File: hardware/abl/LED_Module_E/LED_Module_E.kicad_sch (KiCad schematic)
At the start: 97 parts, among them J1 SFW20S-2STE1LF, J3 009159008603906, K1 Conn_01x01, K10 Conn_01x01, K11 Conn_01x01, K12 Conn_01x01, K13 Conn_01x01, K14 Conn_01x01, K15 Conn_01x01, K16 Conn_01x01, K17 Conn_01x01, K18 Conn_01x01, K2 Conn_01x01, K3 Conn_01x01, K4 Conn_01x01, K5 Conn_01x01, K6 Conn_01x01, K7 Conn_01x01, K8 Conn_01x01, K9 Conn_01x01, Q1 Si3456DDV, Q11 Si3456DDV, Q12 Si3456DDV, Q2 Si3456DDV, Q3 Si3456DDV, Q4 Si3456DDV, Q5 Si3456DDV, Q6 Si3456DDV, Q7 Si3456DDV, Q8 Si3456DDV, U2 74HC245, U3 24AA025UIDT-I/OT, U4 74LVC1G32

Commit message: Several small fixes
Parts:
- U3: value 24AA025UIDT-I/OT -> 24AA025E48T-I/OT; LCSC Part # C2061498 -> C129895; Manufacturer_Part_Number 24AA025UIDT-I/OT -> 24AA025E48T-I/OT
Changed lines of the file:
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@@
 			)
 		)
-		(property "Value" "24AA025UIDT-I/OT"
+		(property "Value" "24AA025E48T-I/OT"
 			(at 190.1541 38.735 0)
 			(effects
@@
 			)
 		)
-		(property "Datasheet" "http://ww1.microchip.com/downloads/en/DeviceDoc/21709J.pdf"
+		(property "Datasheet" "https://www.lcsc.com/datasheet/lcsc_datasheet_1810121540_Microchip-Tech-24AA025E48T-I-OT_C129895.pdf"
 			(at 187.96 33.02 0)
 			(effects
@@
 			)
 		)
-		(property "Manufacturer_Part_Number" "24AA025UIDT-I/OT"
+		(property "Manufacturer_Part_Number" "24AA025E48T-I/OT"
 			(at 187.96 45.72 0)
 			(effects
@@
 			)
 		)
-		(property "LCSC Part #" "C2061498"
+		(property "LCSC Part #" "C129895"
 			(at 187.96 45.72 0)
 			(effects

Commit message: Many, many minor updates to the big PCBs, and a few simple helper PCBs.
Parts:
- C4: value 680uF -> 1000uF; LCSC Part # C2760485 -> C487313; Manufacturer_Part_Number RVT1A681M0810 680UF 10V -> VKME1301C102MV
- C5: value 680uF -> 1000uF
- H1, H2, H3, H4, H5, H6, K1, K10, K11, K12, K13, K14, K15, K16, K17, K18, K2, K3, K4, K5, K6, K7, K8, K9, LOGO1, TP1, TP10, TP11, TP12, TP13, TP14, TP2, TP3, TP4, TP5, TP6, TP7, TP8, TP9: now not fitted
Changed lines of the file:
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@@
 		(in_bom no)
 		(on_board yes)
-		(dnp no)
+		(dnp yes)
 		(fields_autoplaced yes)
 		(property "Reference" "H5"
@@
 		(in_bom yes)
 		(on_board yes)
-		(dnp no)
+		(dnp yes)
 		(property "Reference" "TP8"
 			(at 100.33 40.005 0)
@@
 		(in_bom no)
 		(on_board yes)
-		(dnp no)
+		(dnp yes)
 		(fields_autoplaced yes)
 		(property "Reference" "H4"
@@
 		(in_bom yes)
 		(on_board yes)
-		(dnp no)
+		(dnp yes)
 		(fields_autoplaced yes)
 		(property "Reference" "K12"
@@
 		(in_bom yes)
 		(on_board yes)
-		(dnp no)
+		(dnp yes)
 		(fields_autoplaced yes)
 		(property "Reference" "K6"
@@
 		(in_bom yes)
 		(on_board yes)
-		(dnp no)
+		(dnp yes)
 		(fields_autoplaced yes)
 		(property "Reference" "K18"
@@
 		(in_bom yes)
 		(on_board yes)
-		(dnp no)
+		(dnp yes)
 		(property "Reference" "TP7"
 			(at 100.33 27.305 0)
@@
 		(in_bom yes)
 		(on_board yes)
-		(dnp no)
+		(dnp yes)
 		(property "Reference" "TP10"
 			(at 100.33 65.405 0)
@@
 		(in_bom yes)
 		(on_board yes)
-		(dnp no)
+		(dnp yes)
 		(fields_autoplaced yes)
 		(property "Reference" "K3"
@@
 		(in_bom yes)
 		(on_board yes)
-		(dnp no)
+		(dnp yes)
 		(fields_autoplaced yes)
 		(property "Reference" "K11"
@@
 		(in_bom yes)
 		(on_board yes)
-		(dnp no)
+		(dnp yes)
 		(fields_autoplaced yes)
 		(property "Reference" "K7"
@@
 		(in_bom yes)
 		(on_board yes)
-		(dnp no)
+		(dnp yes)
 		(fields_autoplaced yes)
 		(property "Reference" "K13"
@@
 		(in_bom yes)
 		(on_board yes)
-		(dnp no)
+		(dnp yes)
 		(property "Reference" "TP14"
 			(at 100.33 116.205 0)
@@
 		(in_bom yes)
 		(on_board yes)
-		(dnp no)
+		(dnp yes)
 		(fields_autoplaced yes)
 		(property "Reference" "K8"
@@
 		(in_bom no)
 		(on_board yes)
-		(dnp no)
+		(dnp yes)
 		(fields_autoplaced yes)
 		(property "Reference" "H2"
@@
 		(in_bom yes)
 		(on_board yes)
-		(dnp no)
+		(dnp yes)
 		(fields_autoplaced yes)
 		(property "Reference" "K15"
@@
 		(in_bom yes)
 		(on_board yes)
-		(dnp no)
+		(dnp yes)
 		(fields_autoplaced yes)
 		(property "Reference" "K17"
@@
 			)
 		)
-		(property "Value" "680uF"
+		(property "Value" "1000uF"
 			(at 151.765 37.8459 0)
 			(effects
@@
 			)
 		)
-		(property "Manufacturer_Part_Number" "RVT1A681M0810 680UF 10V"
+		(property "Manufacturer_Part_Number" "VKME1301C102MV"
 			(at 148.59 37.465 0)
 			(effects
@@
 			)
 		)
-		(property "LCSC Part #" "C2760485"
+		(property "LCSC Part #" "C487313"
 			(at 148.59 37.465 0)
 			(effects
@@
 		(in_bom yes)
 		(on_board yes)
-		(dnp no)
+		(dnp yes)
 		(fields_autoplaced yes)
 		(property "Reference" "K4"
@@
 		(in_bom yes)
 		(on_board yes)
-		(dnp no)
+		(dnp yes)
 		(property "Reference" "TP13"
 			(at 100.33 102.235 0)
@@
 		(in_bom yes)
 		(on_board yes)
-		(dnp no)
+		(dnp yes)
 		(property "Reference" "TP11"
 			(at 100.33 76.835 0)
@@
 		(in_bom no)
 		(on_board yes)
-		(dnp no)
+		(dnp yes)
 		(fields_autoplaced yes)
 		(property "Reference" "H3"
@@
 		(in_bom yes)
 		(on_board yes)
-		(dnp no)
+		(dnp yes)
 		(fields_autoplaced yes)
 		(property "Reference" "K9"
@@
 		(in_bom no)
 		(on_board yes)
-		(dnp no)
+		(dnp yes)
 		(fields_autoplaced yes)
 		(property "Reference" "H1"
@@
 			)
 		)
-		(property "Value" "680uF"
+		(property "Value" "1000uF"
 			(at 132.715 38.1 0)
 			(effects
@@
 		(in_bom no)
 		(on_board yes)
-		(dnp no)
+		(dnp yes)
 		(fields_autoplaced yes)
 		(property "Reference" "H6"
@@
 		(in_bom yes)
 		(on_board yes)
-		(dnp no)
+		(dnp yes)
 		(fields_autoplaced yes)
 		(property "Reference" "K2"
@@
 		(in_bom yes)
 		(on_board yes)
-		(dnp no)
+		(dnp yes)
 		(fields_autoplaced yes)
 		(property "Reference" "K14"
@@
 		(in_bom yes)
 		(on_board yes)
-		(dnp no)
+		(dnp yes)
 		(fields_autoplaced yes)
 		(property "Reference" "K10"
@@
 		(in_bom yes)
 		(on_board yes)
-		(dnp no)
+		(dnp yes)
 		(property "Reference" "TP12"
 			(at 100.33 90.805 0)
@@
 		(in_bom yes)
 		(on_board yes)
-		(dnp no)
+		(dnp yes)
 		(property "Reference" "TP3"
 			(at 109.855 164.465 0)
@@
 		(in_bom yes)
 		(on_board yes)
-		(dnp no)
+		(dnp yes)
 		(property "Reference" "TP5"
 			(at 121.285 164.465 0)
@@
 		(in_bom yes)
 		(on_board yes)
-		(dnp no)
+		(dnp yes)
 		(fields_autoplaced yes)
 		(property "Reference" "K1"
@@
 		(in_bom yes)
 		(on_board yes)
-		(dnp no)
+		(dnp yes)
 		(property "Reference" "TP9"
 			(at 100.33 52.705 0)
@@
 		(in_bom yes)
 		(on_board yes)
-		(dnp no)
+		(dnp yes)
 		(property "Reference" "TP2"
 			(at 104.14 164.465 0)
@@
 		(in_bom yes)
 		(on_board yes)
-		(dnp no)
+		(dnp yes)
 		(property "Reference" "TP4"
 			(at 115.57 164.465 0)
@@
 		(in_bom yes)
 		(on_board yes)
-		(dnp no)
+		(dnp yes)
 		(property "Reference" "TP6"
 			(at 127 164.465 0)
@@
 		(in_bom yes)
 		(on_board yes)
-		(dnp no)
+		(dnp yes)
 		(fields_autoplaced yes)
 		(property "Reference" "K5"
@@
 		(in_bom yes)
 		(on_board yes)
-		(dnp no)
+		(dnp yes)
 		(property "Reference" "TP1"
 			(at 99.06 164.465 0)
@@
 		(in_bom yes)
 		(on_board yes)
-		(dnp no)
+		(dnp yes)
 		(fields_autoplaced yes)
 		(property "Reference" "K16"
@@
 		(in_bom no)
 		(on_board yes)
-		(dnp no)
+		(dnp yes)
 		(fields_autoplaced yes)
 		(property "Reference" "LOGO1"

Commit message: Many small adjustments for the next production run.
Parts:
- removed TP1, TP2, TP3, TP4: TestPoint, TestPoint:TestPoint_Pad_D1.0mm, symbol Connector:TestPoint
- added H7, H8: MountingHole_Pad, MountingHole:MountingHole_2.5mm_Pad_TopOnly, symbol Mechanical:MountingHole_Pad
- C5: LCSC Part # C2760485 -> C487313; Manufacturer_Part_Number RVT1A681M0810 680UF 10V -> VKME1301C102MV
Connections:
- net +5V is gone; now on net +4V: C2.1, J1.13, J3.4, U2.20 (VCC)
- net GND: now also H7.1, H8.1

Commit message: Add missing LCSC part numbers and bump version / date.
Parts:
- J1: LCSC Part # C5407823 -> C3168412
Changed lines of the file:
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@@
 			)
 		)
-		(property "LCSC Part #" "C5407823"
+		(property "LCSC Part #" "C3168412"
 			(at 246.38 52.07 0)
 			(effects

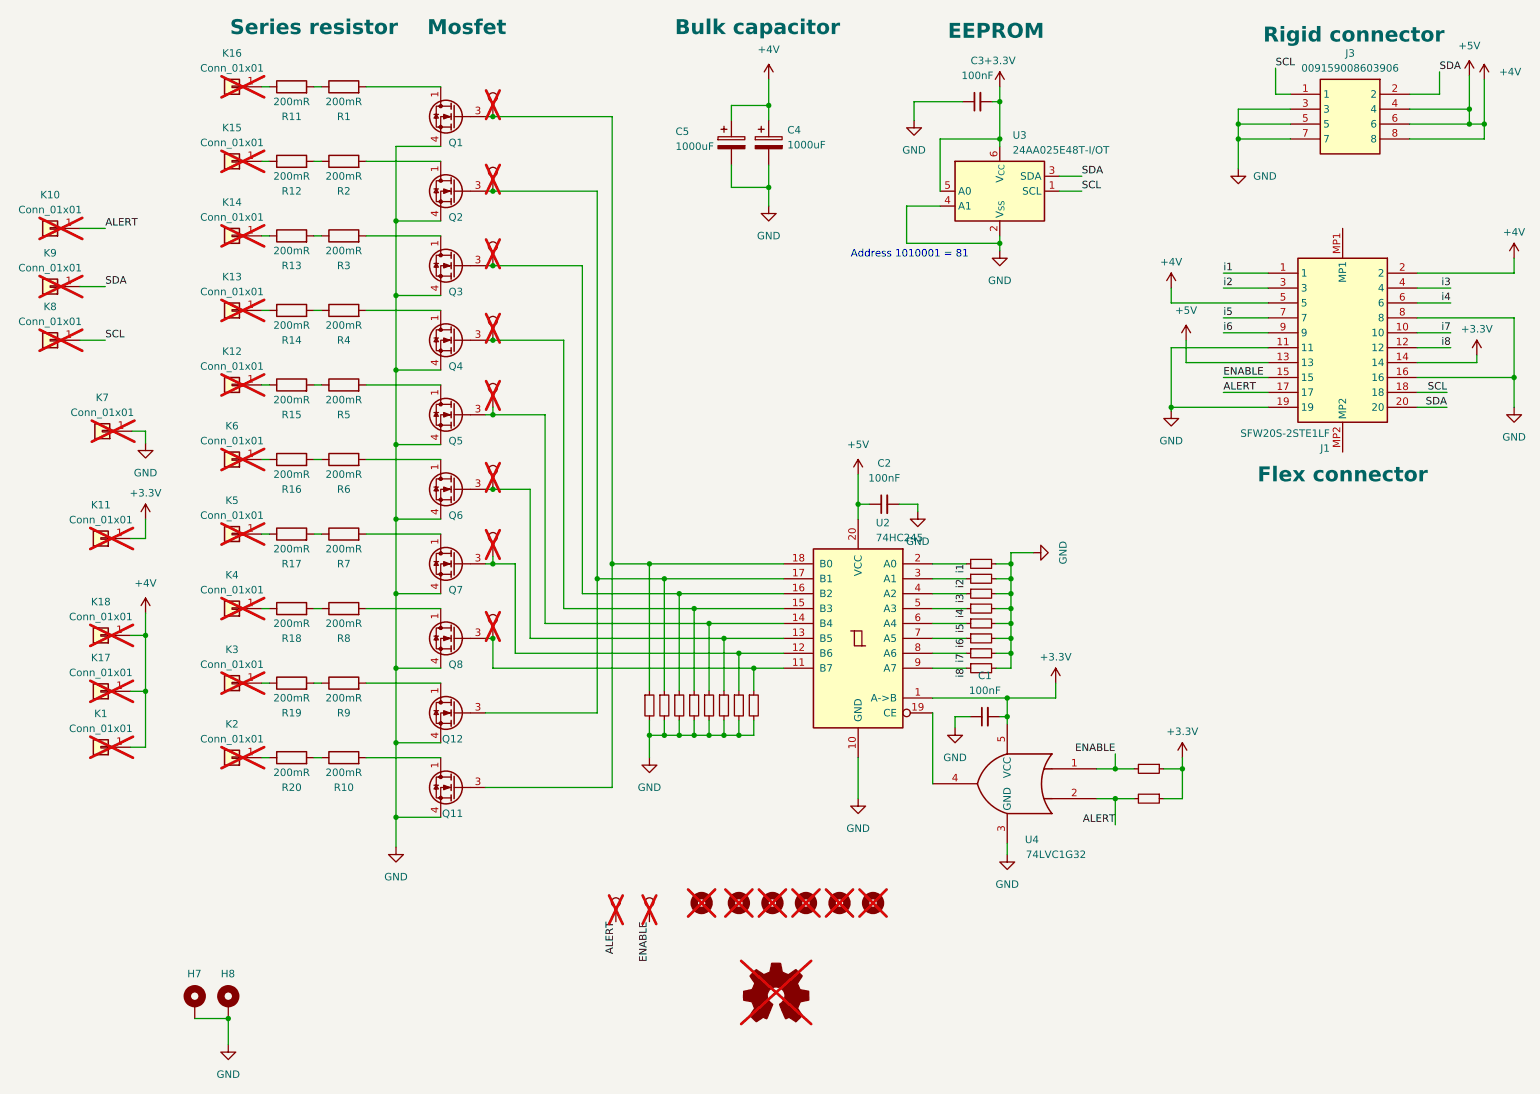
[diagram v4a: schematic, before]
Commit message: Update files and documentation for LED modules E and G.
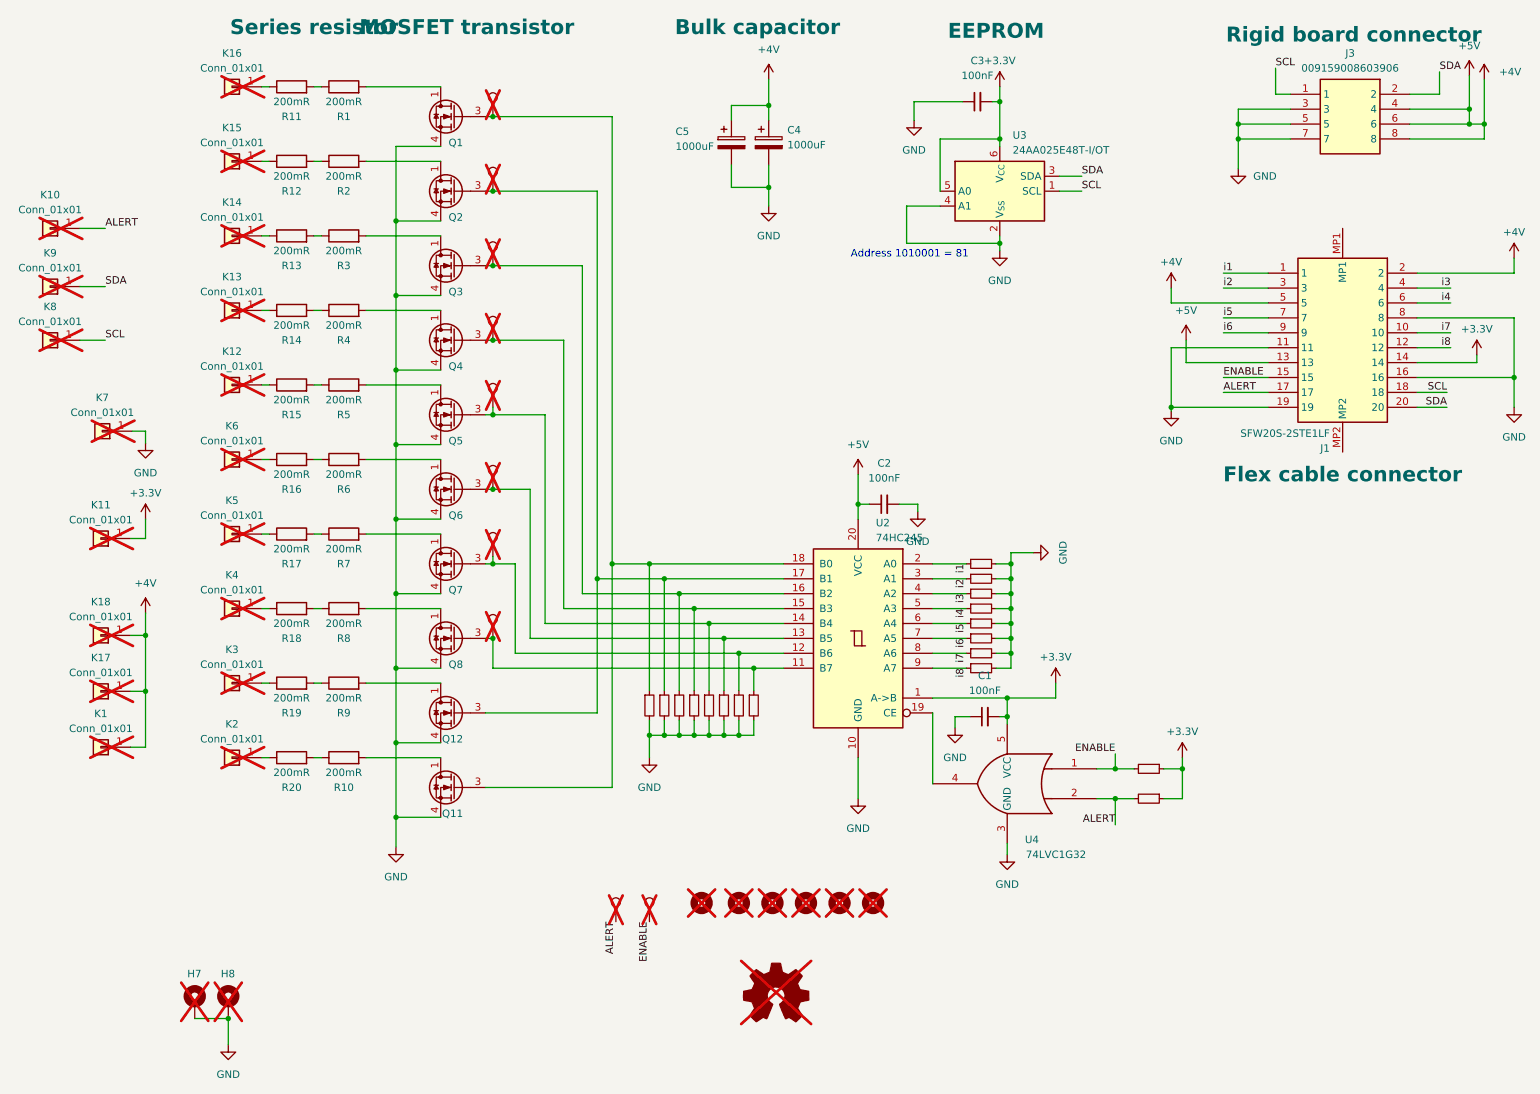
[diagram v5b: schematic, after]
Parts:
- C1, C2, C3: Manufacturer_Part_Number (none) -> CL05B104KO5NNNC
- H7, H8: now not fitted
- J1: Purpose Flex connector -> Flex cable connector
- J3: LCSC Part # (none) -> C22394454; Purpose Rigid connector -> Rigid board connector
- Q1, Q11, Q12, Q2, Q3, Q4, Q5, Q6, Q7, Q8: LCSC Part # C145273 -> C6295864; Manufacturer_Part_Number SI3456DDV-T1-GE3 -> SI3456DDV-T1-BE3; Purpose Mosfet -> MOSFET transistor
- R21, R22, R23, R24, R25, R26, R27, R28, R31, R32, R33, R34, R35, R36, R37, R38: LCSC Part # (none) -> C25900; Manufacturer_Part_Number (none) -> 0402WGF4701TCE; Purpose Pullup -> Pullup resistor
- R40, R41: Purpose Pullup -> Pullup resistor
- U2: Purpose (none) -> Bus transceivers / line driver
- U4: Purpose (none) -> Logic OR gate

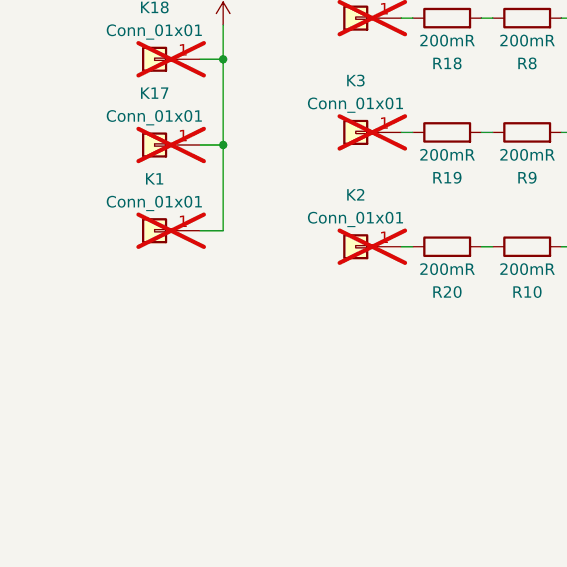
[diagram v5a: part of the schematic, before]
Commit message: LED Module E version 4.0: two rows of castellated holes instead of one, for larger pitch and easier soldering. Also optimized routing.
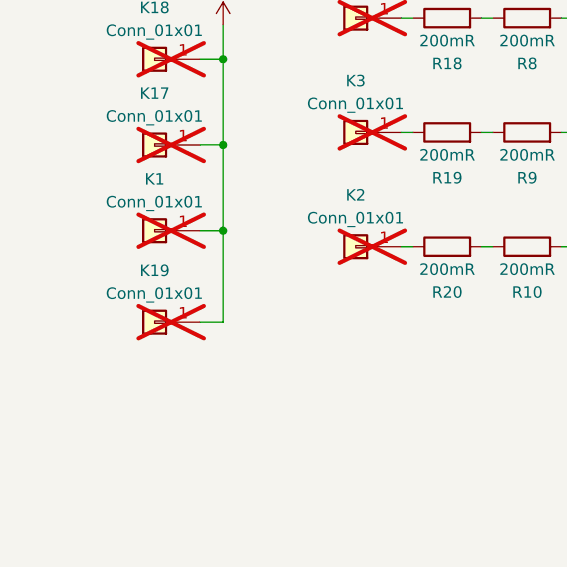
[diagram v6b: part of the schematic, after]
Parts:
- added K19: Conn_01x01, TestPoint:TestPoint_THTPad_1.0x1.0mm_Drill0.5mm, symbol Connector_Generic:Conn_01x01
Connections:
- net +4V: now also K19.1 (Pin_1)
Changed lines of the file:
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@@
 	(title_block
 		(title "besteLampe! LED Module E")
-		(date "2024-12-01")
-		(rev "3.0")
+		(date "2025-09-13")
+		(rev "4.0")
 		(comment 1 "See  https://lenaschimmel.de/besteLampe! for the source and more information")
 		(comment 2 "This source describes Open Hardware and is licensed under the CERN-OHL-S v2.")
@@
 	)
 	(junction
+		(at 42.418 140.462)
+		(diameter 0)
+		(color 0 0 0 0)
+	)
+	(junction
 		(at 101.6 33.02)
 		(diameter 0)
@@
 	(wire
 		(pts
+			(xy 42.418 150.622) (xy 42.418 140.462)
+		)
+		(stroke
+			(width 0)
+			(type default)
+		)
+	)
+	(wire
+		(pts
 			(xy 80.01 91.44) (xy 92.71 91.44)
 		)
@@
 	(wire
 		(pts
+			(xy 39.878 150.622) (xy 42.418 150.622)
+		)
+		(stroke
+			(width 0)
+			(type default)
+		)
+	)
+	(wire
+		(pts
 			(xy 219.075 149.225) (xy 215.9 149.225)
 		)
@@
 					(unit 1)
 				)
+			)
+		)
+	)
+	(symbol
+		(lib_id "Connector_Generic:Conn_01x01")
+		(at 34.798 150.622 180)
+		(unit 1)
+		(exclude_from_sim no)
+		(in_bom yes)
+		(on_board yes)
+		(dnp yes)
+		(fields_autoplaced yes)
+		(property "Reference" "K19"
+			(at 34.798 144.907 0)
+			(effects
+				(font
+					(size 1.27 1.27)
+				)
+			)
+		)
+		(property "Value" "Conn_01x01"
+			(at 34.798 147.447 0)
+			(effects
+				(font
+					(size 1.27 1.27)
+				)
+			)
+		)
+		(property "Footprint" "TestPoint:TestPoint_THTPad_1.0x1.0mm_Drill0.5mm"
+			(at 34.798 150.622 0)
+			(effects
+				(font
+					(size 1.27 1.27)
+				)
+				(hide yes)
+			)
+		)
+		(property "Datasheet" "~"
+			(at 34.798 150.622 0)
+			(effects
+				(font
+					(size 1.27 1.27)
+				)
+				(hide yes)
+			)
+		)
+		(property "Description" "Generic connector, single row, 01x01, script generated (kicad-library-utils/schlib/autogen/connector/)"
+			(at 34.798 150.622 0)
+			(effects
+				(font
+					(size 1.27 1.27)
+				)
+				(hide yes)
+			)
+		)
+		(pin "1"
+		)
+		(instances
+			(project "LED_Module_E"
+				(path "/271a71a9-d0cc-4466-ad75-113fb931f3c8"
+					(reference "K19")
+					(unit 1)
+				)
